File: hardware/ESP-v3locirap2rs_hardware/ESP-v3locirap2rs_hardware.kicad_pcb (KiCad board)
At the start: 2 copper layers, 1 part

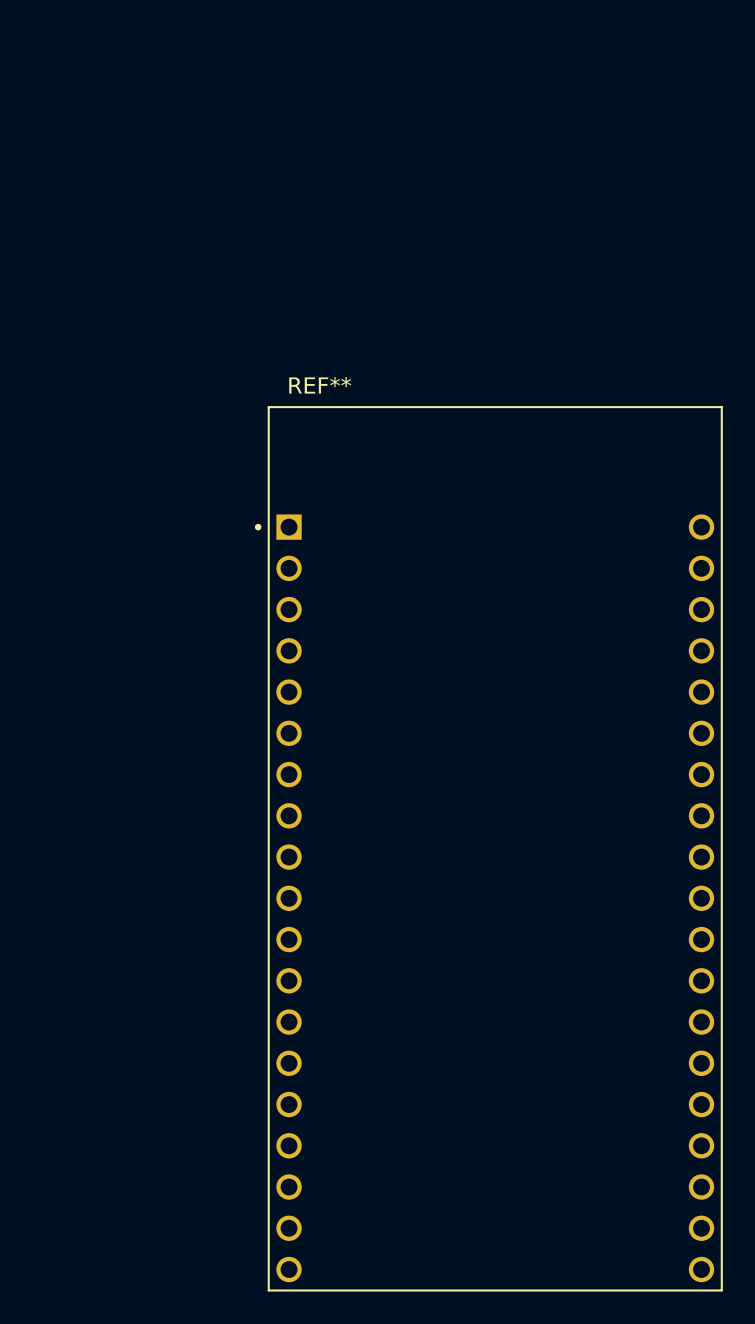
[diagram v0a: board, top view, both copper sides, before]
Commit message: kicad schematic updates
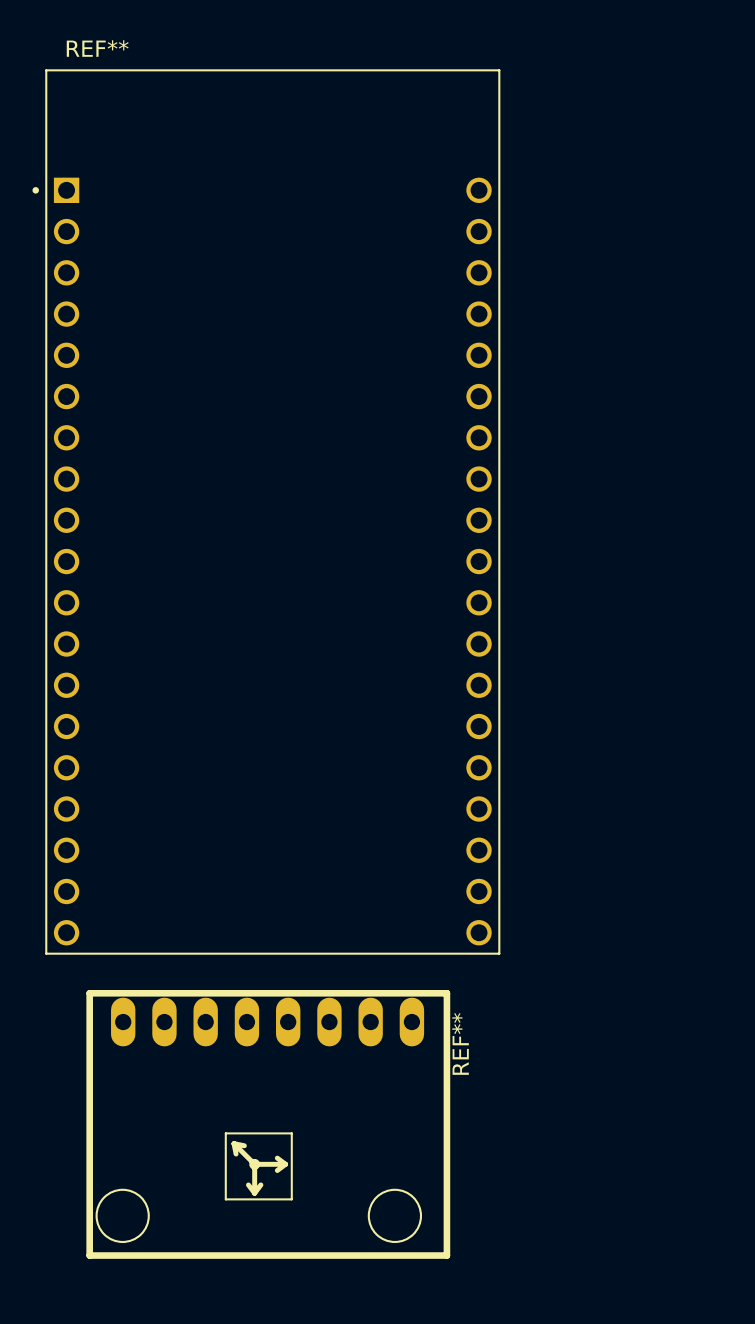
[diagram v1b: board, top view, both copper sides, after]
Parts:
- added REF**: GY-521, ESP-v3locirap2rs_footprints:GY-521, F.Cu at (124.5, 106.9)
- moved REF** 24.9 mm to (135.8, 77.3)

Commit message: pcb updates
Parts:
- removed REF**: MODULE_ESP32-DEVKITC-32D, digikey-footprints:MODULE_ESP32-DEVKITC-32D
- removed REF**: GY-521, ESP-v3locirap2rs_footprints:GY-521
- added ACC1: GY-521, ESP-v3locirap2rs_footprints:GY-521, F.Cu at (127.4, 90.5)
- added U1: ESP32-DEVKITC-32D, ESP-v3locirap2rs_footprints:MODULE_ESP32-DEVKITC-32D, F.Cu at (106.8, 82.6)

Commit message: circuit wiring
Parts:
- moved ACC1 41.0 mm to (93.4, 113.2), turned to -90 degrees
- moved U1 2.60 mm to (104.2, 82.6)
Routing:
- net /ESP32/3.3V: track 0.00 -> 66.6 mm, vias 0 -> 1
- net /ESP32/SCL: track 0.00 -> 50.7 mm
- net /ESP32/SDA: track 0.00 -> 49.6 mm
- net GND: track 0.00 -> 28.2 mm

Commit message: kicad pcb updates
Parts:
- moved ACC1 8.36 mm to (101.5, 111.4)
- moved U1 8.32 mm to (112.5, 82.0), turned to 180 degrees
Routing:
- net /ESP32/3.3V: track 66.6 -> 0.00 mm, vias 1 -> 0
- net /ESP32/SCL: track 50.7 -> 0.00 mm
- net /ESP32/SDA: track 49.6 -> 0.00 mm
- net GND: track 28.2 -> 0.00 mm
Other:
- board outline added: 32 x 77 mm

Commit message: pcb v1 completed
added cool velociraptor graphic too (rawr)
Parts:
- added G***: LOGO, ESP-v3locirap2rs_footprints:v3locirap2rs_graphic, B.Cu at (112.5, 122.7)
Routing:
- net GND: track 0.00 -> 47.1 mm
- net /ESP32/SDA: track 0.00 -> 37.1 mm, vias 0 -> 1
- net /ESP32/SCL: track 0.00 -> 24.4 mm
- net /ESP32/3.3V: track 0.00 -> 13.0 mm
- net unconnected-(ACC1-PadXCL): track 0.09 -> 0.64 mm
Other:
- board text added: "32"

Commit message: updates
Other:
- board size 32 x 77 mm -> 53.5 x 77 mm
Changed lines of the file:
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@@
 	(gr_poly
 		(pts
-			(xy 96.5 54.5) (xy 98.5 52.5) (xy 112.5 52.5) (xy 126.5 52.5) (xy 128.5 54.5) (xy 128.5 119) (xy 125 129.5)
+			(xy 96.5 54.5) (xy 98.5 52.5) (xy 112.5 52.5) (xy 147.5 52.5) (xy 150 54.5) (xy 150 119.25) (xy 146.5 129.5)
 			(xy 100 129.5) (xy 96.5 119)
 		)

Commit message: PCB completed
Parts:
- added BAT1: BC9VPC, Battery:BatteryHolder_Eagle_12BH611-GR, F.Cu at (95.2, 103.7)
- added DS1: WC1602A, Display:WC1602A, F.Cu at (159.2, 123.7)
- added R1: 1k, Resistor_SMD:R_0805_2012Metric, F.Cu at (108.6, 127.3)
- added R2: 1.2k, Resistor_SMD:R_0805_2012Metric, F.Cu at (111.5, 127.3)
- added U2: L7805CV, Package_TO_SOT_THT:TO-220-3_Vertical, F.Cu at (107.5, 118.8)
- G***: moved to F.Cu
- moved ACC1 27.9 mm to (129.3, 114.2)
- moved U1 24.9 mm to (137.2, 79.0)
- moved G*** 22.5 mm to (90.0, 122.5), turned to 0 degrees
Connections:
- U1 pad J2-19: unconnected-(U1-EXT_5V-PadJ2-19) -> /ESP32/5V
- U1 pad J3-11: unconnected-(U1-IO17-PadJ3-11) -> /ESP32/Pin 17
- U1 pad J3-12: unconnected-(U1-IO16-PadJ3-12) -> /ESP32/Pin 16
- U1 pad J3-16: unconnected-(U1-IO15-PadJ3-16) -> /ESP32/Pin 15
- U1 pad J3-2: unconnected-(U1-IO23-PadJ3-2) -> /ESP32/Pin 23
- U1 pad J3-8: unconnected-(U1-IO19-PadJ3-8) -> /ESP32/Pin 19
- U1 pad J3-9: unconnected-(U1-IO18-PadJ3-9) -> /ESP32/Pin 18
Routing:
- net /ESP32/5V: track 0.00 -> 128.5 mm
- net GND: track 47.1 -> 146.5 mm
- net Net-(DS1-LED(+)): track 0.00 -> 88.9 mm, vias 0 -> 1
- net /ESP32/Pin 19: track 0.00 -> 68.4 mm, vias 0 -> 1
- net /ESP32/Pin 15: track 0.00 -> 61.3 mm, vias 0 -> 1
- net Net-(DS1-VO): track 0.00 -> 59.1 mm
- net /ESP32/Pin 17: track 0.00 -> 56.8 mm, vias 0 -> 1
- net /ESP32/Pin 18: track 0.00 -> 53.6 mm, vias 0 -> 1
- net /ESP32/Pin 16: track 0.00 -> 52.8 mm, vias 0 -> 1
- net /ESP32/Pin 23: track 0.00 -> 45.4 mm
- net Net-(U2-IN): track 0.00 -> 20.2 mm
- net /ESP32/SCL: track 24.4 -> 41.0 mm, vias 0 -> 1
- net /ESP32/3.3V: track 13.0 -> 17.6 mm
- net unconnected-(ACC1-PadXCL): track 0.64 -> 0.00 mm
- net /ESP32/SDA: track 37.1 -> 36.9 mm, vias 1 -> 0
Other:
- board size 53.5 x 77 mm -> 115.2 x 85 mm

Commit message: pcb & schematic updates
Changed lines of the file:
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@@
 		(fp_arc
 			(start 64.20104 22.49932)
-			(mid 64.054473 22.853115)
+			(mid 64.054479 22.85315)
 			(end 63.70066 22.9997)
 			(stroke
